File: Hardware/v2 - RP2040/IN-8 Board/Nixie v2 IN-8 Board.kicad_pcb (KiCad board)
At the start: 2 copper layers, 26 parts, among them J1 Conn_01x10_Pin, J2 Conn_01x10_Pin, J3 Conn_01x10_Pin, Q1 MMBTA42, Q2 PZTA92, U1 NCH8200HV, U3 К155ИД1, U4 К155ИД1, U5 К155ИД1, U6 К155ИД1

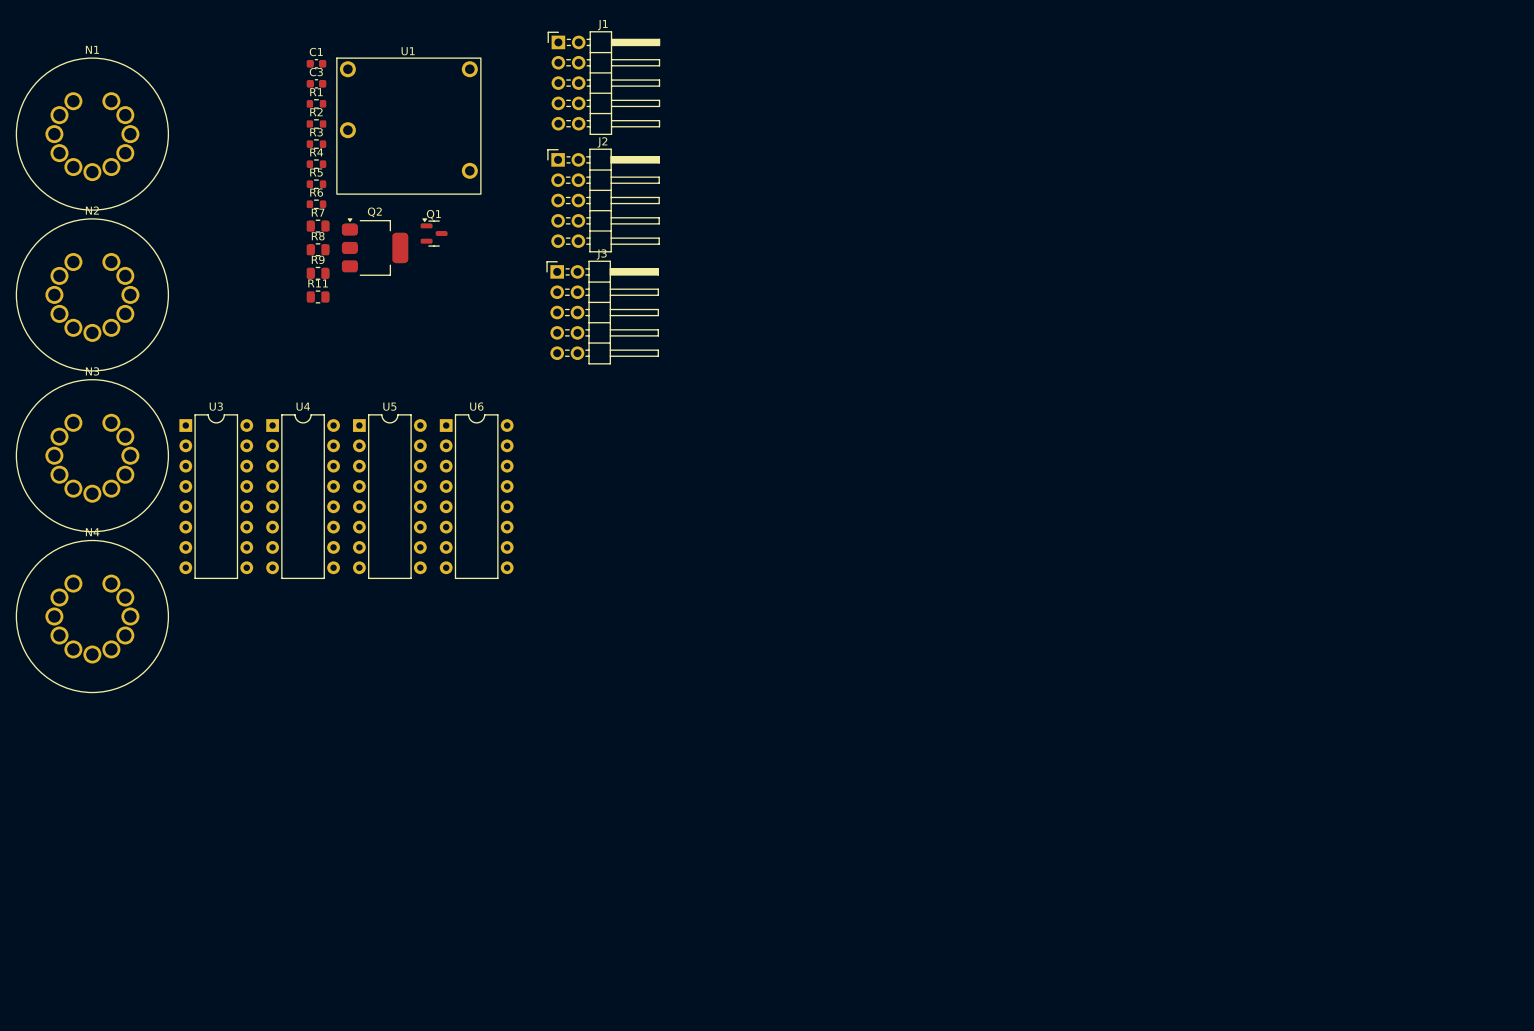
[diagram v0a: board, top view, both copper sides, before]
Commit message: Started board layout
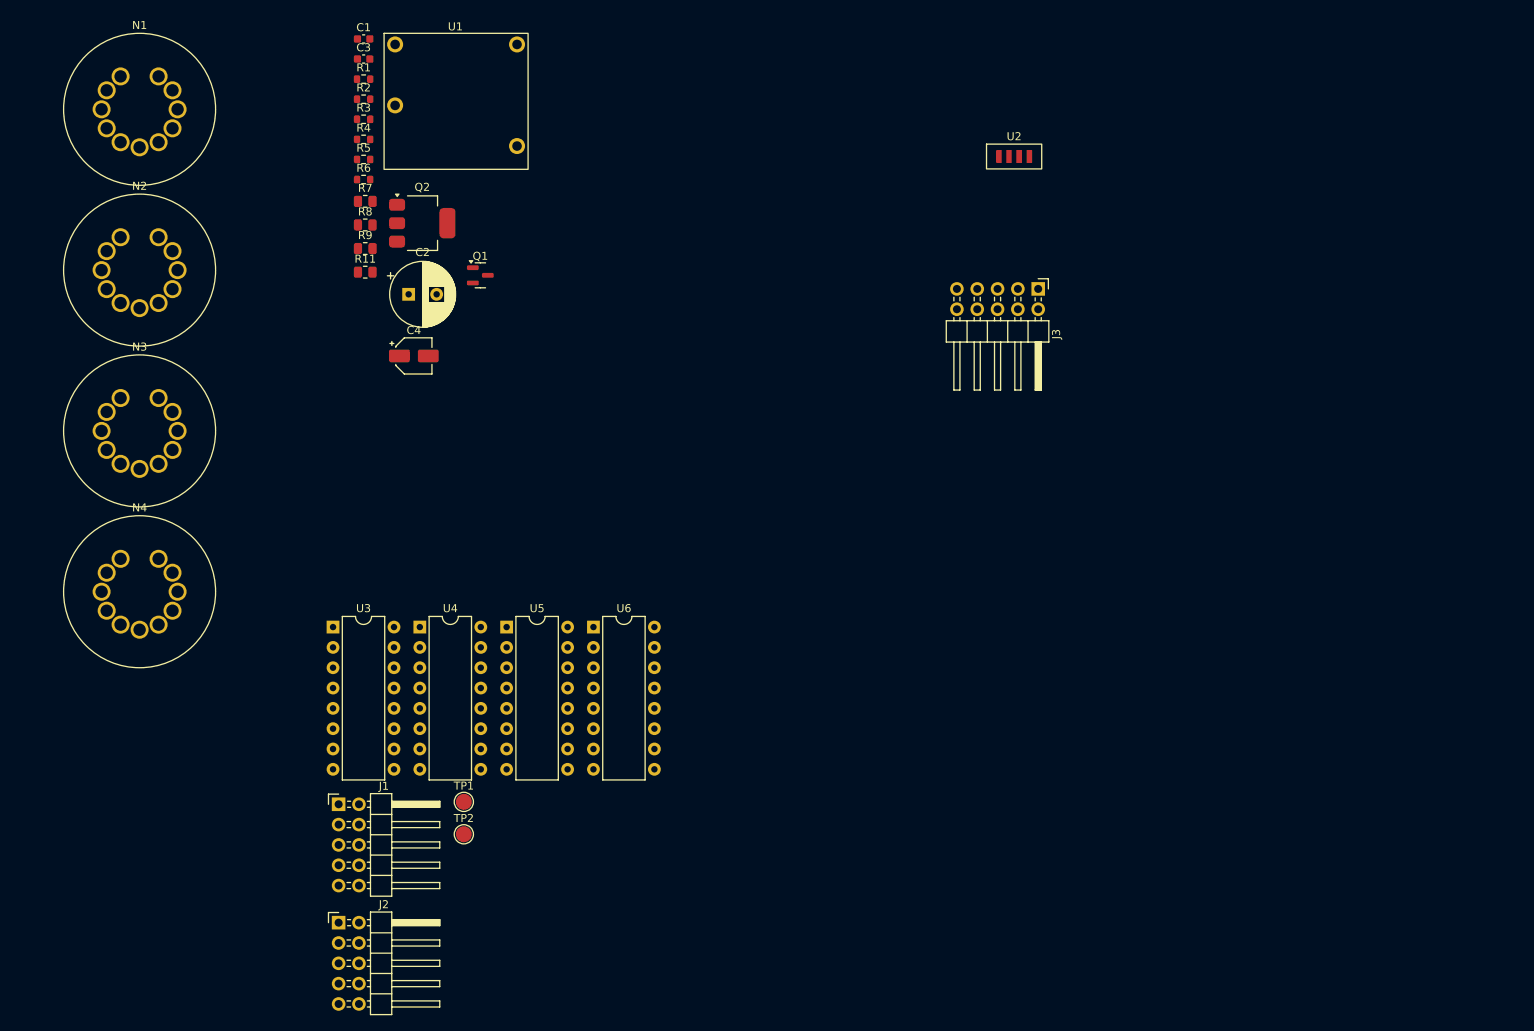
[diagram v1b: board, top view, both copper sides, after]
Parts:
- added C2: 4.7u, Capacitor_THT:CP_Radial_D8.0mm_P3.50mm, F.Cu at (71.3, 53.2)
- added C4: 10u, Capacitor_SMD:CP_Elec_4x5.4, F.Cu at (71.9, 60.9)
- added TP1: TestPoint, TestPoint:TestPoint_Pad_D2.0mm, F.Cu at (78.2, 116.7)
- added TP2: TestPoint, TestPoint:TestPoint_Pad_D2.0mm, F.Cu at (78.2, 120.7)
- added U2: VEML7700, Nick_Sensors:VEML7700-TV, F.Cu at (147.0, 36.0)
- moved J2 99.2 mm to (62.5, 131.8)
- moved J1 99.1 mm to (62.5, 117.0)
- moved J3 60.2 mm to (150.0, 52.5), turned to -90 degrees
- moved U3 31.2 mm to (61.8, 94.8)
- moved U4 31.2 mm to (72.7, 94.8)
- moved U5 31.2 mm to (83.5, 94.8)
- moved U6 31.2 mm to (94.4, 94.8)
- moved Q1 7.80 mm to (80.2, 50.9)
- moved Q2 6.66 mm to (73.0, 44.3)
- moved R11 6.66 mm to (65.9, 50.5)
- moved R7 6.66 mm to (65.9, 41.6)
- moved R8 6.66 mm to (65.9, 44.6)
- moved U1 6.66 mm to (77.1, 29.7)
- moved N3 6.66 mm to (37.6, 70.3)
- moved R9 6.66 mm to (65.9, 47.5)
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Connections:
- J1 pad 1: GND -> /Hours_Ones_B
- J1 pad 10: GND -> /Hours_Tens_A
- J1 pad 2: /Hours_Tens_A -> /Hours_Ones_C
- J1 pad 3: /Hours_Tens_D -> /Hours_Ones_A
- J1 pad 4: /Hours_Tens_B -> /Hours_Ones_D
- J1 pad 5: /Hours_Tens_C -> GND
- J1 pad 6: /Hours_Ones_C -> GND
- J1 pad 7: /Hours_Ones_B -> /Hours_Tens_C
- J1 pad 8: /Hours_Ones_D -> /Hours_Tens_B
- J1 pad 9: /Hours_Ones_A -> /Hours_Tens_D
- J2 pad 1: GND -> /Minutes_Ones_B
- J2 pad 10: GND -> /Minutes_Tens_A
- J2 pad 2: /Minutes_Tens_A -> /Minutes_Ones_C
- J2 pad 3: /Minutes_Tens_D -> /Minutes_Ones_A
- J2 pad 4: /Minutes_Tens_B -> /Minutes_Ones_D
- J2 pad 5: /Minutes_Tens_C -> GND
- J2 pad 6: /Minutes_Ones_C -> GND
- J2 pad 7: /Minutes_Ones_B -> /Minutes_Tens_C
- J2 pad 8: /Minutes_Ones_D -> /Minutes_Tens_B
- J2 pad 9: /Minutes_Ones_A -> /Minutes_Tens_D

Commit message: started nixie layout, added bleed resistor to HV cap
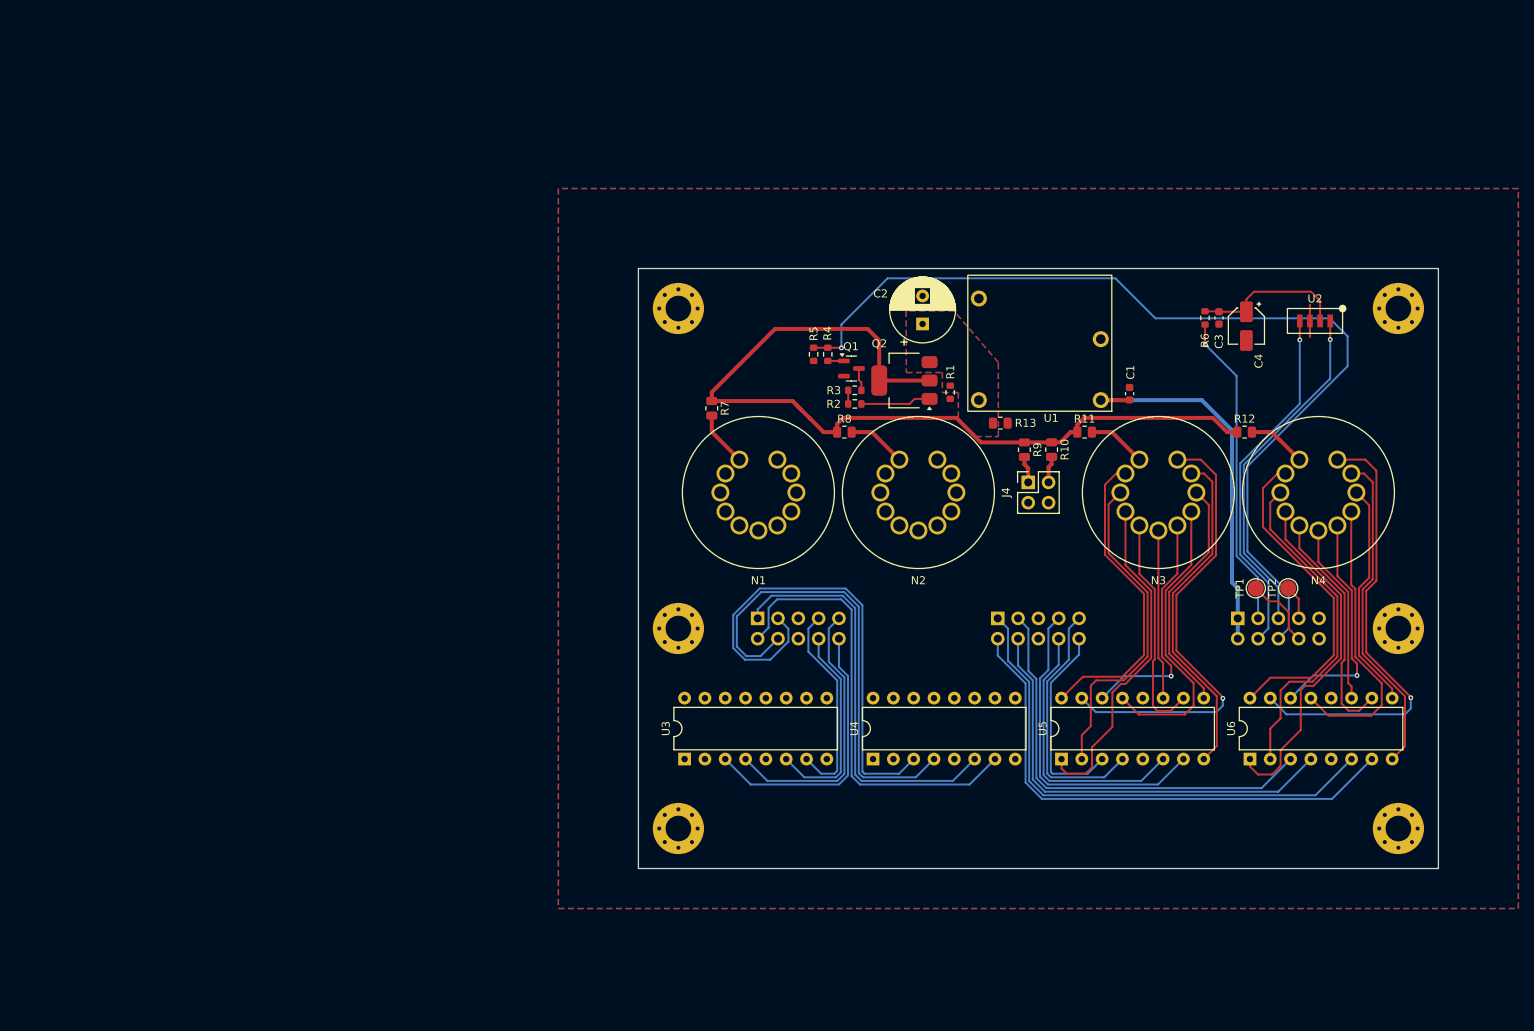
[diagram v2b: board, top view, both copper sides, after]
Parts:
- added H1: MountingHole_Pad, MountingHole:MountingHole_3.2mm_M3_Pad_Via, F.Cu at (105.0, 55.0)
- added H2: MountingHole_Pad, MountingHole:MountingHole_3.2mm_M3_Pad_Via, F.Cu at (195.0, 55.0)
- added H3: MountingHole_Pad, MountingHole:MountingHole_3.2mm_M3_Pad_Via, F.Cu at (195.0, 95.0)
- added H4: MountingHole_Pad, MountingHole:MountingHole_3.2mm_M3_Pad_Via, F.Cu at (105.0, 95.0)
- added H5: MountingHole_Pad, MountingHole:MountingHole_3.2mm_M3_Pad_Via, F.Cu at (195.0, 120.0)
- added H6: MountingHole_Pad, MountingHole:MountingHole_3.2mm_M3_Pad_Via, F.Cu at (105.0, 120.0)
- added J4: Conn_02x02_Odd_Even, Connector_PinSocket_2.54mm:PinSocket_2x02_P2.54mm_Vertical, F.Cu at (148.7, 76.7)
- added R10: 22k, Resistor_SMD:R_0805_2012Metric, F.Cu at (151.7, 72.6)
- added R13: 100k, Resistor_SMD:R_0805_2012Metric, F.Cu at (145.2, 69.3)
- added R9: 22k, Resistor_SMD:R_0805_2012Metric, F.Cu at (148.2, 72.7)
- J1, J2, J3: footprint Connector_PinHeader_2.54mm:PinHeader_2x05_P2.54mm_Horizontal -> Connector_PinHeader_2.54mm:PinHeader_2x05_P2.54mm_Vertical; moved to B.Cu
- moved N4 147.9 mm to (185.0, 78.0)
- moved N3 127.6 mm to (165.0, 78.0)
- moved R12 111.7 mm to (175.8, 70.5)
- moved C3 111.7 mm to (172.6, 56.2), turned to -90 degrees
- moved TP2 107.5 mm to (181.2, 90.0), turned to 90 degrees
- moved R6 106.6 mm to (170.8, 56.2), turned to -90 degrees
- moved C1 105.5 mm to (161.4, 65.7), turned to 90 degrees
- moved C4 104.1 mm to (176.0, 57.2), turned to -90 degrees
- moved TP1 102.5 mm to (177.2, 90.0), turned to 90 degrees
- moved N2 101.2 mm to (135.0, 78.0)
- moved R11 92.8 mm to (155.8, 70.5)
- moved N1 91.0 mm to (115.0, 78.0)
- moved J2 90.7 mm to (144.9, 93.7), turned to -90 degrees
- moved U6 83.7 mm to (176.4, 111.3), turned to 90 degrees
- moved R1 83.1 mm to (139.0, 65.5), turned to -90 degrees
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- renumbered R9 to R11, R11 to R12
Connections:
- C2 pad 1: Net-(Q2-E) -> /170V
- Q2 pad 3: Net-(Q2-E) -> /170V
- R1 pad 1: Net-(Q2-E) -> /170V
- U1 pad 2: GND -> /170V
- U1 pad 3: Net-(Q2-E) -> GND
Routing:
- net /DIMMING: track 0.00 -> 120.7 mm, vias 0 -> 1
- net /ANODE: track 0.00 -> 110.6 mm
- net /Minutes_Ones_C: track 0.00 -> 65.6 mm
- net /Minutes_Ones_B: track 0.00 -> 64.9 mm
- net /Hours_Ones_A: track 0.00 -> 62.5 mm
- net /Hours_Ones_D: track 0.00 -> 58.9 mm
- net Net-(U5-1): track 0.00 -> 57.6 mm, vias 0 -> 1
- net Net-(U6-1): track 0.00 -> 56.7 mm, vias 0 -> 1
- net /Hours_Ones_C: track 0.00 -> 56.2 mm
- net /Minutes_Ones_D: track 0.00 -> 55.5 mm
- net /Minutes_Ones_A: track 0.00 -> 54.7 mm
- net /Hours_Ones_B: track 0.00 -> 51.8 mm
- net VBUS: track 0.00 -> 47.9 mm
- net /I2C1_SDA: track 0.00 -> 44.8 mm, vias 0 -> 1
- net Net-(U6-8): track 0.00 -> 44.0 mm
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- added copper zone on B.Cu, net /170V
- added copper zone on F.Cu, net /170V
- added copper zone on B.Cu, net GND
- added copper zone on F.Cu, net GND
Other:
- board outline added: 100 x 75 mm

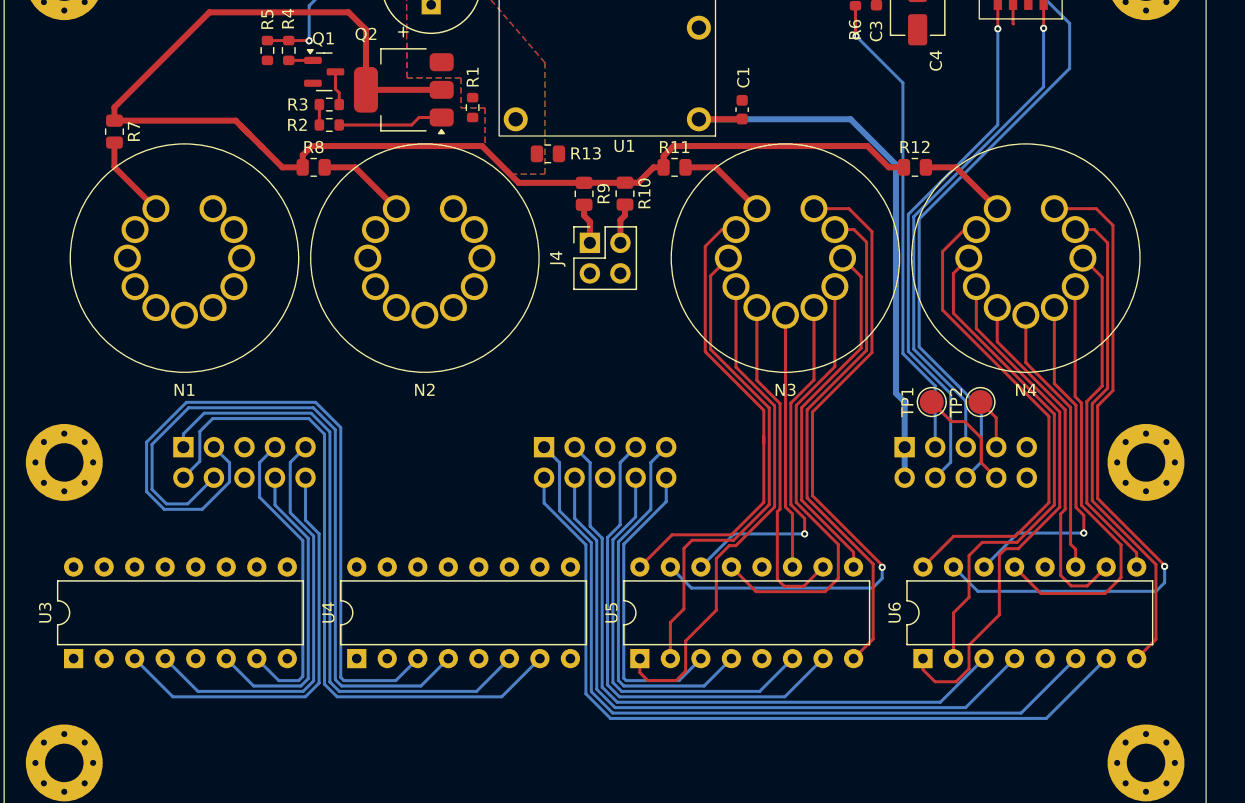
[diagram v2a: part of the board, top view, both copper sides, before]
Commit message: Completed initial layout of the IN-8 board
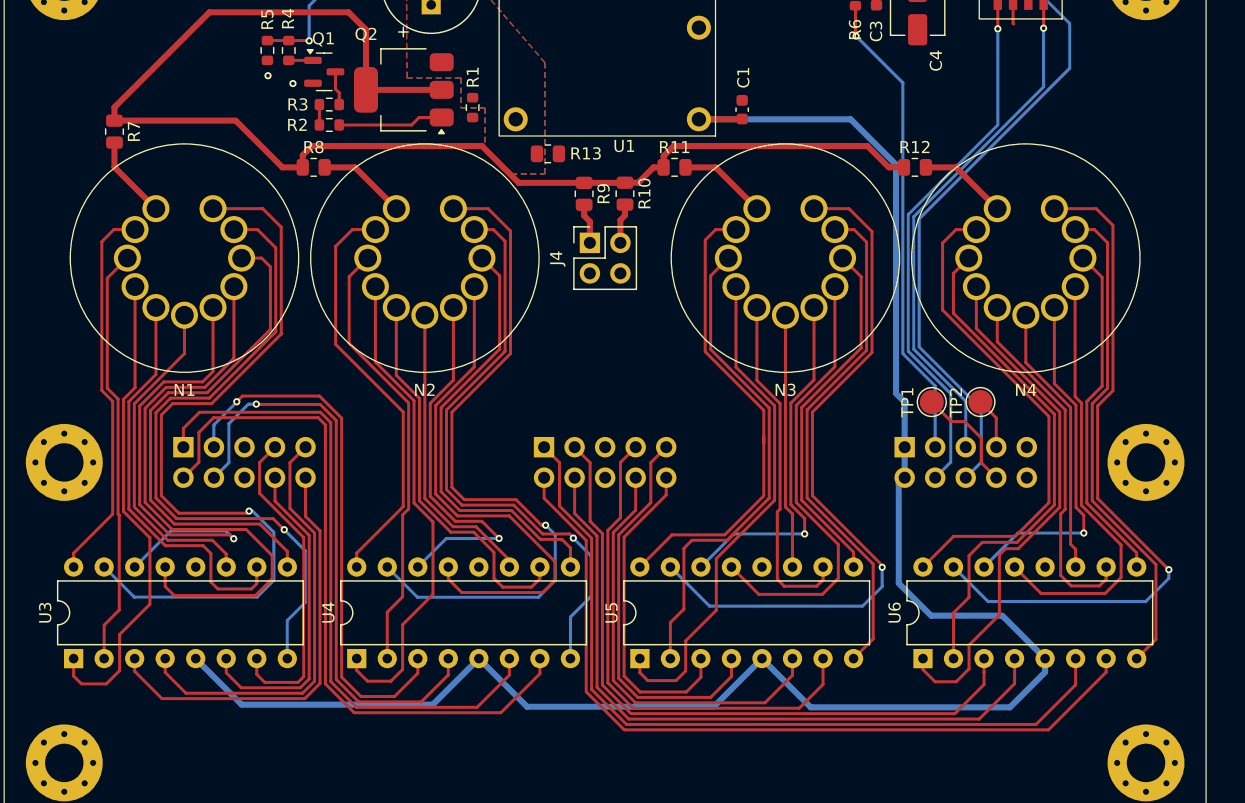
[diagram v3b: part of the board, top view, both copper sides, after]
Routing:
- net VBUS: track 47.9 -> 152.9 mm
- net Net-(U3-1): track 0.00 -> 65.2 mm, vias 0 -> 1
- net Net-(U4-1): track 0.00 -> 58.5 mm, vias 0 -> 1
- net Net-(U3-2): track 0.00 -> 54.8 mm, vias 0 -> 1
- net Net-(U4-2): track 0.00 -> 49.3 mm, vias 0 -> 1
- net Net-(U3-4): track 0.00 -> 48.7 mm
- net Net-(U4-4): track 0.00 -> 43.2 mm
- net Net-(U3-3): track 0.00 -> 42.6 mm
- net Net-(U4-8): track 0.00 -> 40.5 mm
- net Net-(U3-8): track 0.00 -> 40.3 mm
- net Net-(U3-5): track 0.00 -> 39.6 mm, vias 0 -> 1
- net Net-(U4-9): track 0.00 -> 36.7 mm
- net Net-(U4-3): track 0.00 -> 36.4 mm
- net Net-(U3-9): track 0.00 -> 34.9 mm
- net Net-(N2-0): track 0.00 -> 34.5 mm
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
